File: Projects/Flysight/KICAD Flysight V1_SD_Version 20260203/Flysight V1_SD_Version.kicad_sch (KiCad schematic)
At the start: 0 parts

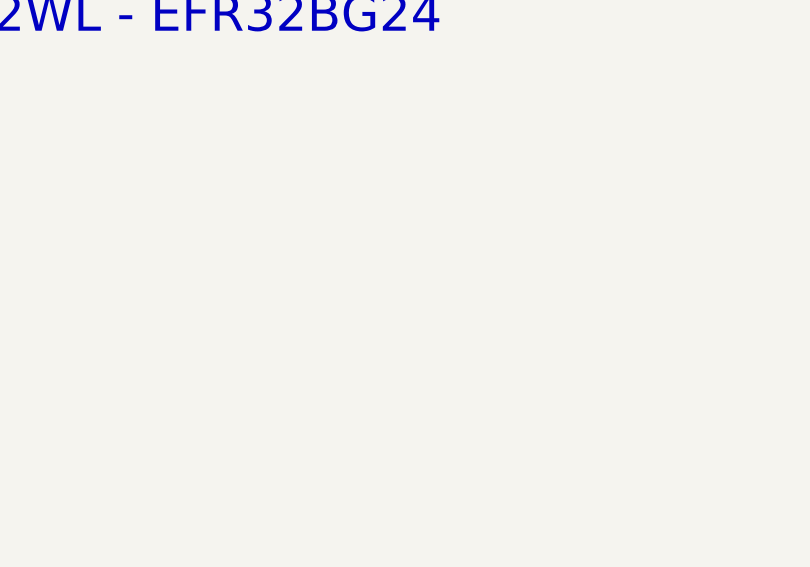
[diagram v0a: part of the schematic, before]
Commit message: Commit 2: PaginaMock Added
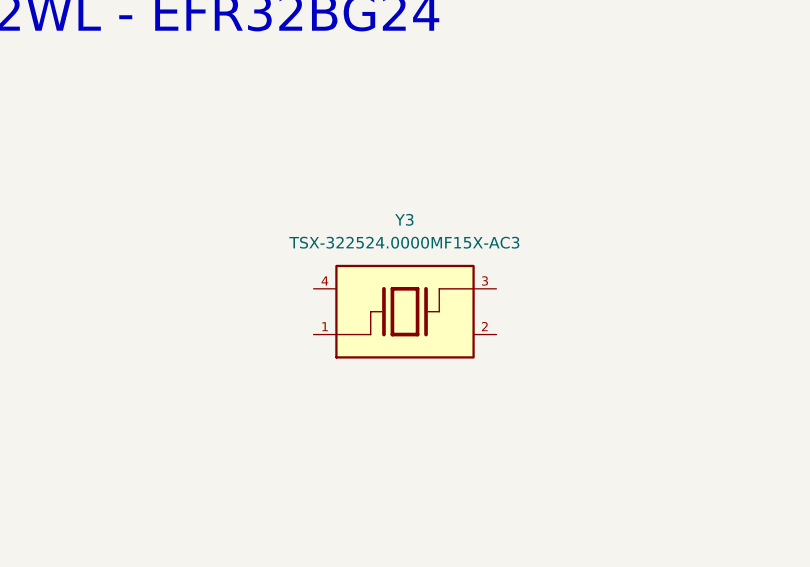
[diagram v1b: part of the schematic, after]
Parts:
- added Y3: TSX-322524.0000MF15X-AC3, TSX-322524.0000MF15X-AC3:OSCCC320X250X60, symbol Osc:TSX-322524.0000MF15X-AC3
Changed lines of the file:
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@@
+		)
+	)
+	(symbol
+		(lib_id "Osc:TSX-322524.0000MF15X-AC3")
+		(at 132.08 218.44 0)
+		(unit 1)
+		(exclude_from_sim no)
+		(in_bom yes)
+		(on_board yes)
+		(dnp no)
+		(fields_autoplaced yes)
+		(property "Reference" "Y3"
+			(at 132.08 208.28 0)
+			(effects
+				(font
+					(size 1.27 1.27)
+				)
+			)
+		)
+		(property "Value" "TSX-322524.0000MF15X-AC3"
+			(at 132.08 210.82 0)
+			(effects
+				(font
+					(size 1.27 1.27)
+				)
+			)
+		)
+		(property "Footprint" "TSX-322524.0000MF15X-AC3:OSCCC320X250X60"
+			(at 132.08 218.44 0)
+			(effects
+				(font
+					(size 1.27 1.27)
+				)
+				(justify bottom)
+				(hide yes)
+			)
+		)
+		(property "Datasheet" ""
+			(at 132.08 218.44 0)
+			(effects
+				(font
+					(size 1.27 1.27)
+				)
+				(hide yes)
+			)
+		)
+		(property "Description" ""
+			(at 132.08 218.44 0)
+			(effects
+				(font
+					(size 1.27 1.27)
+				)
+				(hide yes)
+			)
+		)
+		(property "PARTREV" "N/A"
+			(at 132.08 218.44 0)
+			(effects
+				(font
+					(size 1.27 1.27)
+				)
+				(justify bottom)
+				(hide yes)
+			)
+		)
+		(property "MANUFACTURER" "Seiko Epson Corporation"
+			(at 132.08 218.44 0)
+			(effects
+				(font
+					(size 1.27 1.27)
+				)
+				(justify bottom)
+				(hide yes)
+			)
+		)
+		(property "MAXIMUM_PACKAGE_HEIGHT" "0.6 mm"
+			(at 132.08 218.44 0)
+			(effects
+				(font
+					(size 1.27 1.27)
+				)
+				(justify bottom)
+				(hide yes)
+			)
+		)
+		(property "STANDARD" "IPC 7351B"
+			(at 132.08 218.44 0)
+			(effects
+				(font
+					(size 1.27 1.27)
+				)
+				(justify bottom)
+				(hide yes)
+			)
+		)
+		(pin "1"
+		)
+		(pin "2"
+		)
+		(pin "4"
+		)
+		(pin "3"
+		)
+		(instances
+			(project ""
+				(path "/0650c7a8-acba-429c-9f8e-eec0baf0bc1c"
+					(reference "Y3")
+					(unit 1)
+				)
+			)
 		)
 	)
